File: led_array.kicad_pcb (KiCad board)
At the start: 2 copper layers, 49.5 x 49.5 mm, 43 parts, among them IC1 ATMEGA8-P, P1 CONN_02X03

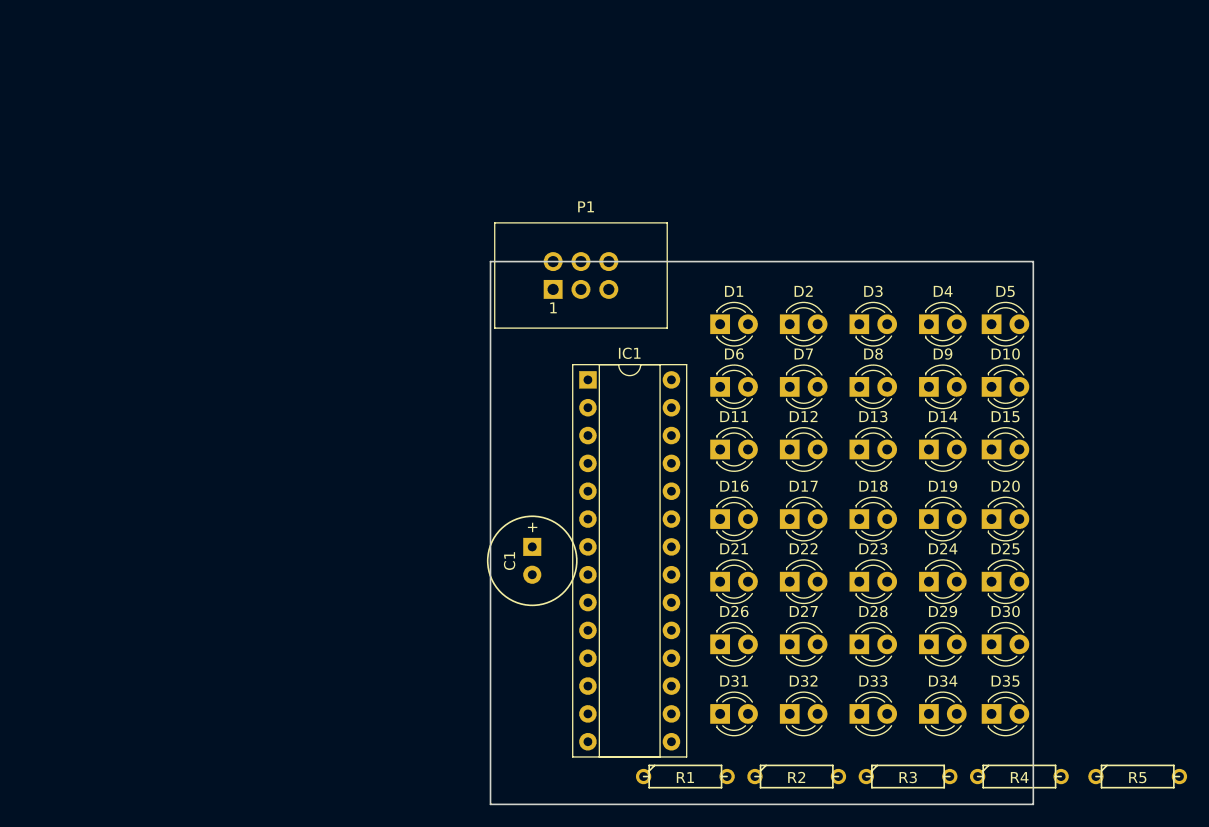
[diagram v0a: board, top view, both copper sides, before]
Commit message: COmpleted routing of LEDs. Other stuff were done before this but I forgot to commit
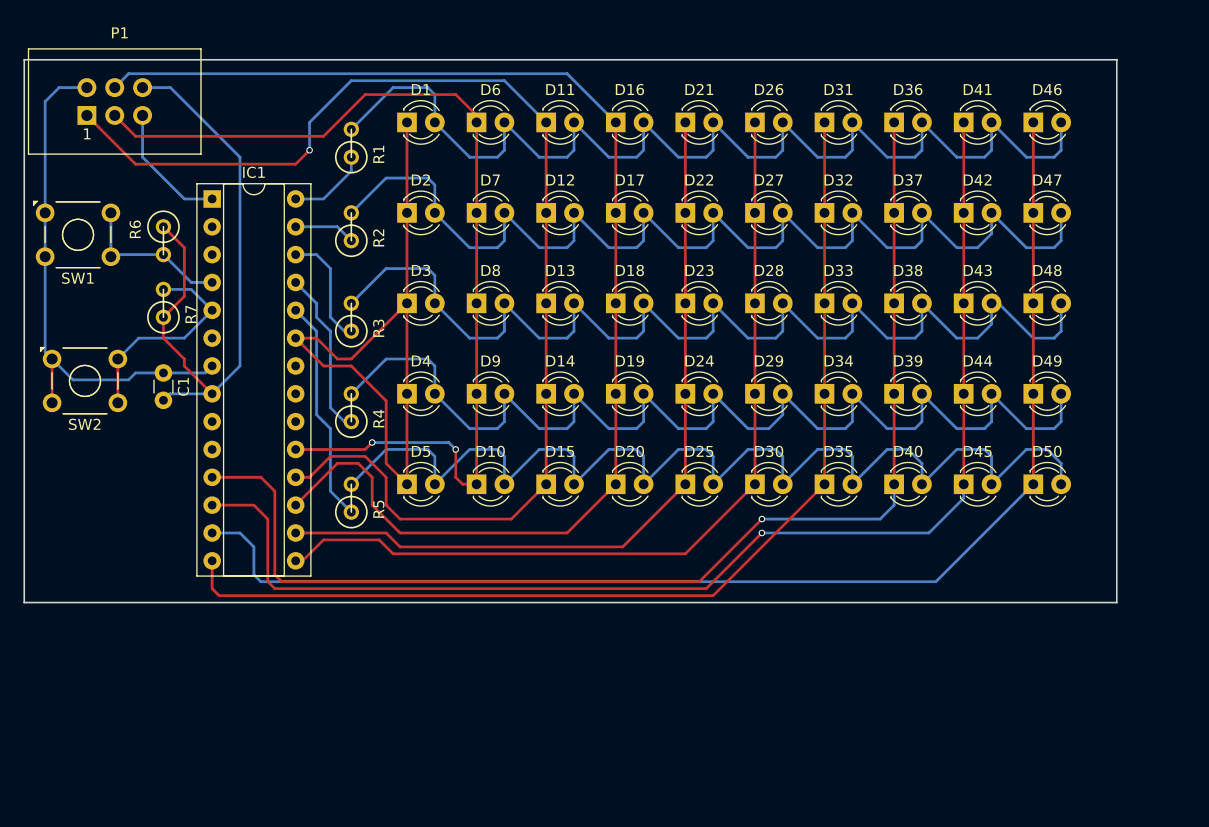
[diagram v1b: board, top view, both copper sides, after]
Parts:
- added D36: LED, LEDs:LED_D3.0mm, F.Cu at (134.0, 38.7)
- added D37: LED, LEDs:LED_D3.0mm, F.Cu at (134.0, 47.0)
- added D38: LED, LEDs:LED_D3.0mm, F.Cu at (134.0, 55.2)
- added D39: LED, LEDs:LED_D3.0mm, F.Cu at (134.0, 63.5)
- added D40: LED, LEDs:LED_D3.0mm, F.Cu at (134.0, 71.8)
- added D41: LED, LEDs:LED_D3.0mm, F.Cu at (140.3, 38.7)
- added D42: LED, LEDs:LED_D3.0mm, F.Cu at (140.3, 47.0)
- added D43: LED, LEDs:LED_D3.0mm, F.Cu at (140.3, 55.2)
- added D44: LED, LEDs:LED_D3.0mm, F.Cu at (140.3, 63.5)
- added D45: LED, LEDs:LED_D3.0mm, F.Cu at (140.3, 71.8)
- added D46: LED, LEDs:LED_D3.0mm, F.Cu at (146.7, 38.7)
- added D47: LED, LEDs:LED_D3.0mm, F.Cu at (146.7, 47.0)
- added D48: LED, LEDs:LED_D3.0mm, F.Cu at (146.7, 55.2)
- added D49: LED, LEDs:LED_D3.0mm, F.Cu at (146.7, 63.5)
- added D50: LED, LEDs:LED_D3.0mm, F.Cu at (146.7, 71.8)
- added R6: 1k, Discret:R1, F.Cu at (67.3, 49.5)
- added R7: 1k, Discret:R1, F.Cu at (67.3, 55.2)
- added SW1: next, Buttons_Switches_THT:SW_TH_Tactile_Omron_B3F-10xx, F.Cu at (56.5, 47.0)
- added SW2: prev, Buttons_Switches_THT:SW_TH_Tactile_Omron_B3F-10xx, F.Cu at (57.1, 60.3)
- C1: value C_Small -> 0.1uF; footprint Discret:C1V8 -> Capacitors_THT:C_Disc_D3.0mm_W1.6mm_P2.50mm
- P1: value CONN_02X03 -> ICSP
- R1, R2, R3, R4, R5: value R_Small -> 220; footprint Discret:R3 -> Discret:R1
- moved R5 76.1 mm to (84.5, 73.0), turned to 90 degrees
- moved R4 69.6 mm to (84.5, 64.8), turned to 90 degrees
- moved R3 65.9 mm to (84.5, 56.5), turned to 90 degrees
- moved R1 65.3 mm to (84.5, 40.6), turned to 90 degrees
- moved R2 64.6 mm to (84.5, 48.3), turned to 90 degrees
- moved D5 55.3 mm to (89.5, 71.8)
- moved D31 54.8 mm to (127.6, 38.7)
- moved D4 48.0 mm to (89.5, 63.5)
- moved D10 47.8 mm to (95.9, 71.8)
- moved D26 47.7 mm to (121.3, 38.7)
- moved D32 45.8 mm to (127.6, 47.0)
- moved P1 45.4 mm to (60.3, 38.1)
- moved D21 42.0 mm to (114.9, 38.7)
- moved D3 41.3 mm to (89.5, 55.2)
- moved D9 41.3 mm to (95.9, 63.5)
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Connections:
- IC1 pad 11: Net-(IC1-Pad11) -> col8
- IC1 pad 12: Net-(IC1-Pad12) -> col9
- IC1 pad 13: Net-(IC1-Pad13) -> col10
- IC1 pad 4: Net-(IC1-Pad4) -> forward
- IC1 pad 5: Net-(IC1-Pad5) -> back
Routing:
- net MOSI: track 0.00 -> 117.9 mm
- net col10: track 0.00 -> 115.0 mm
- net col9: track 0.00 -> 112.8 mm, vias 0 -> 1
- net MISO: track 0.00 -> 111.8 mm, vias 0 -> 1
- net col8: track 0.00 -> 108.5 mm, vias 0 -> 1
- net Net-(D1-Pad2): track 0.00 -> 106.2 mm
- net Net-(D13-Pad2): track 0.00 -> 105.6 mm
- net Net-(D12-Pad2): track 0.00 -> 105.6 mm
- net Net-(D14-Pad2): track 0.00 -> 105.6 mm
- net Net-(D10-Pad2): track 0.00 -> 105.2 mm
- net col7: track 0.00 -> 95.9 mm
- net SCK: track 0.00 -> 89.7 mm, vias 0 -> 2
- net col6: track 0.00 -> 78.9 mm
- net col5: track 0.00 -> 71.5 mm
- net col1: track 0.00 -> 65.1 mm
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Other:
- board size 49.5 x 49.5 mm -> 99.7 x 49.5 mm

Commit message: Small changes made to the schematic
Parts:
- added J1: BARREL_JACK, Connectors:BARREL_JACK, F.Cu at (59.1, 68.6)
- moved P1 1.27 mm to (60.3, 39.4)
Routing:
- net GND: track 58.1 -> 72.8 mm
- net +5V: track 48.0 -> 51.8 mm
- net RST: track 11.7 -> 10.5 mm
- net MOSI: track 117.9 -> 118.9 mm
- net SCK: track 89.7 -> 90.6 mm
- added copper zone on B.Cu, net GND
- added copper zone on F.Cu, net GND
